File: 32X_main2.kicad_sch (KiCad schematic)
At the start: 54 parts, among them IC501 SH2 M, IC502 SH2 S, IC503 µPD4502161, IC504 315-5818, IC506 315-5781, IC507 TC511664, IC508 TC511664, IC509 74AC04, IC510 RHSRL33A

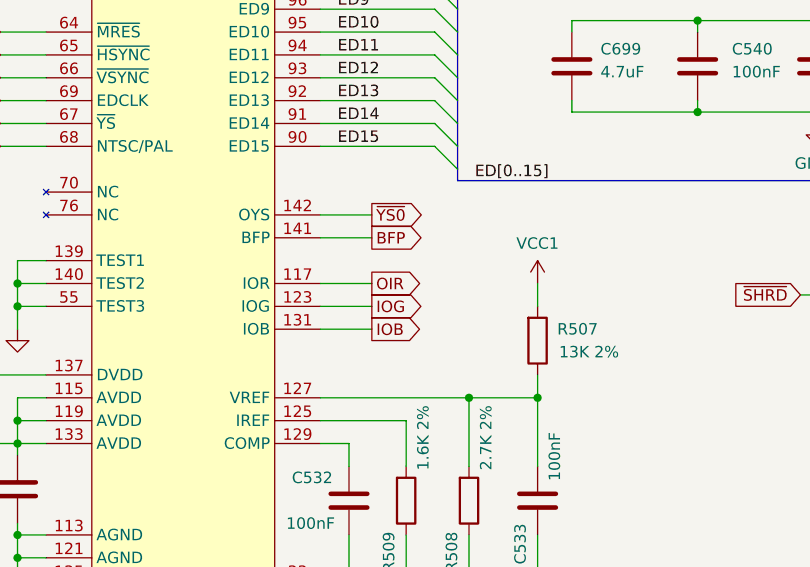
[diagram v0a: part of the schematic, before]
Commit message: Rename OIR -> IOR (issue #20).
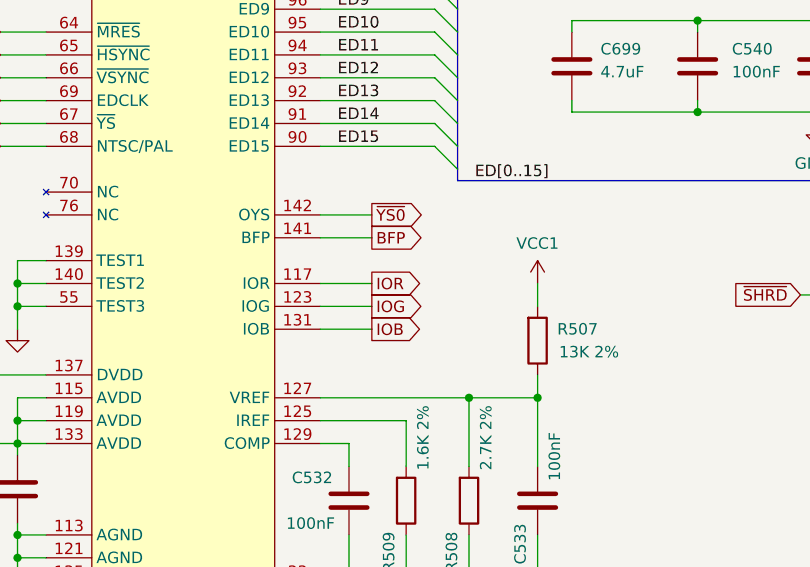
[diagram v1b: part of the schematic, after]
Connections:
- net OIR renamed IOR
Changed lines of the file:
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@@
 		)
 	)
-	(global_label "OIR"
+	(global_label "IOR"
 		(shape output)
 		(at 275.59 231.14 0)
